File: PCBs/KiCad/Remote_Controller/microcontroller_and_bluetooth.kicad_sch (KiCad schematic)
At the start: 19 parts, among them J201 USB_C_Receptacle_USB2.0_16P, Q201 SS8050-G, Q202 SS8050-G, SW201 SW_Push, U201 USBLC6-2SC6, U202 ESP32-WROOM-32E, U203 CH340C

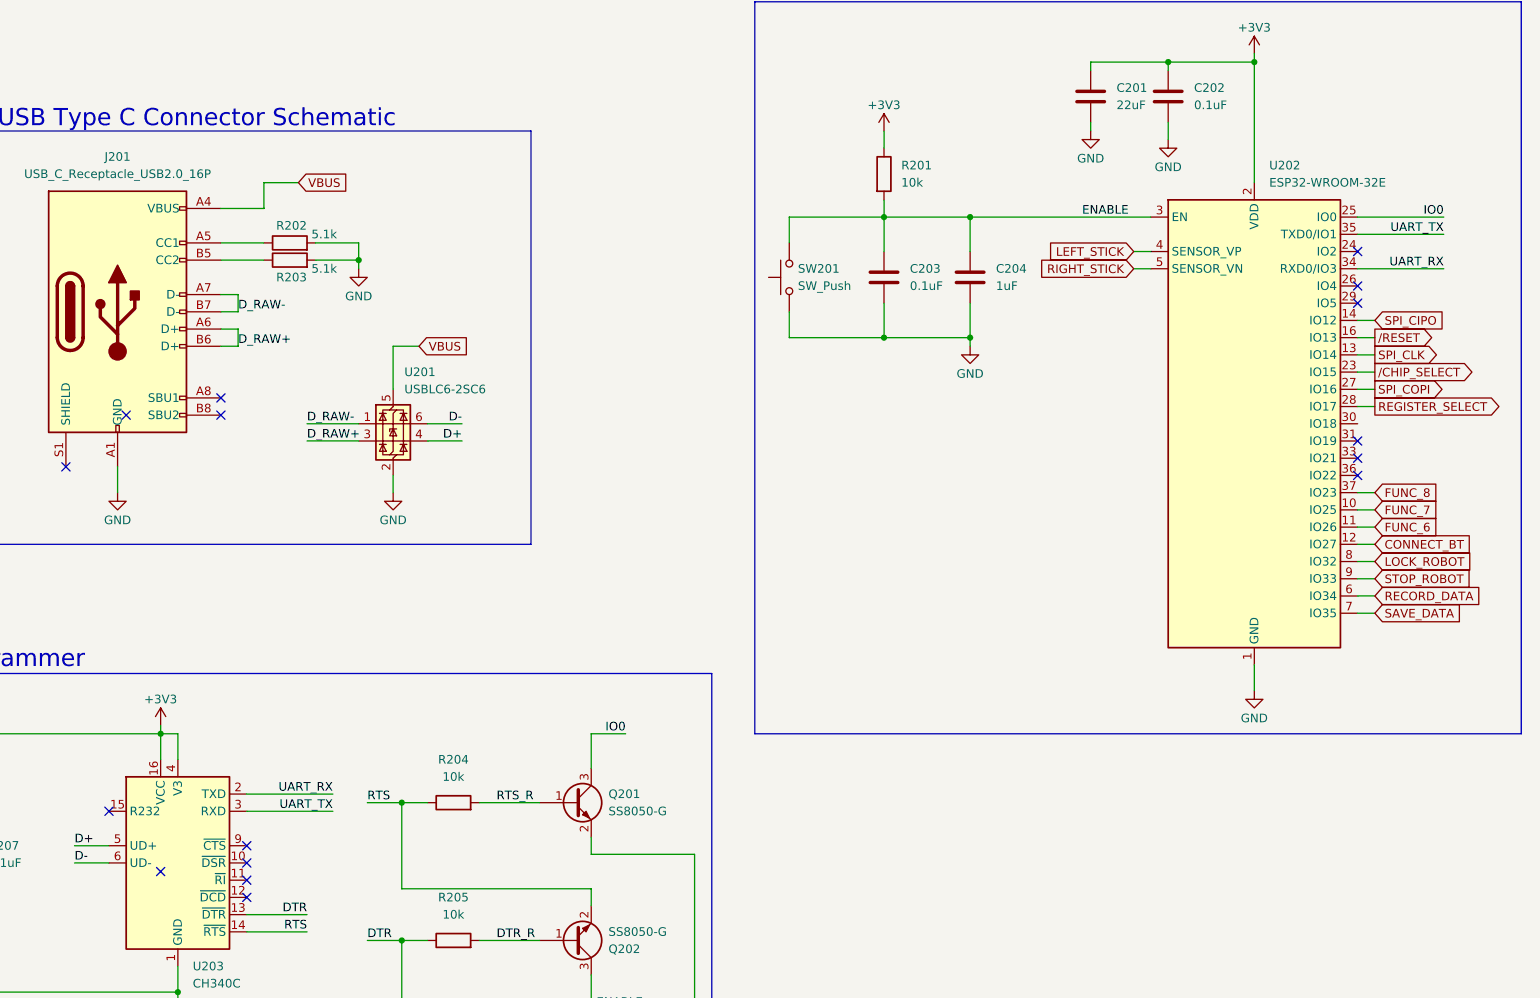
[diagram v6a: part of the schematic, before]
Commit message: Add Joystick footprint and passed ERC
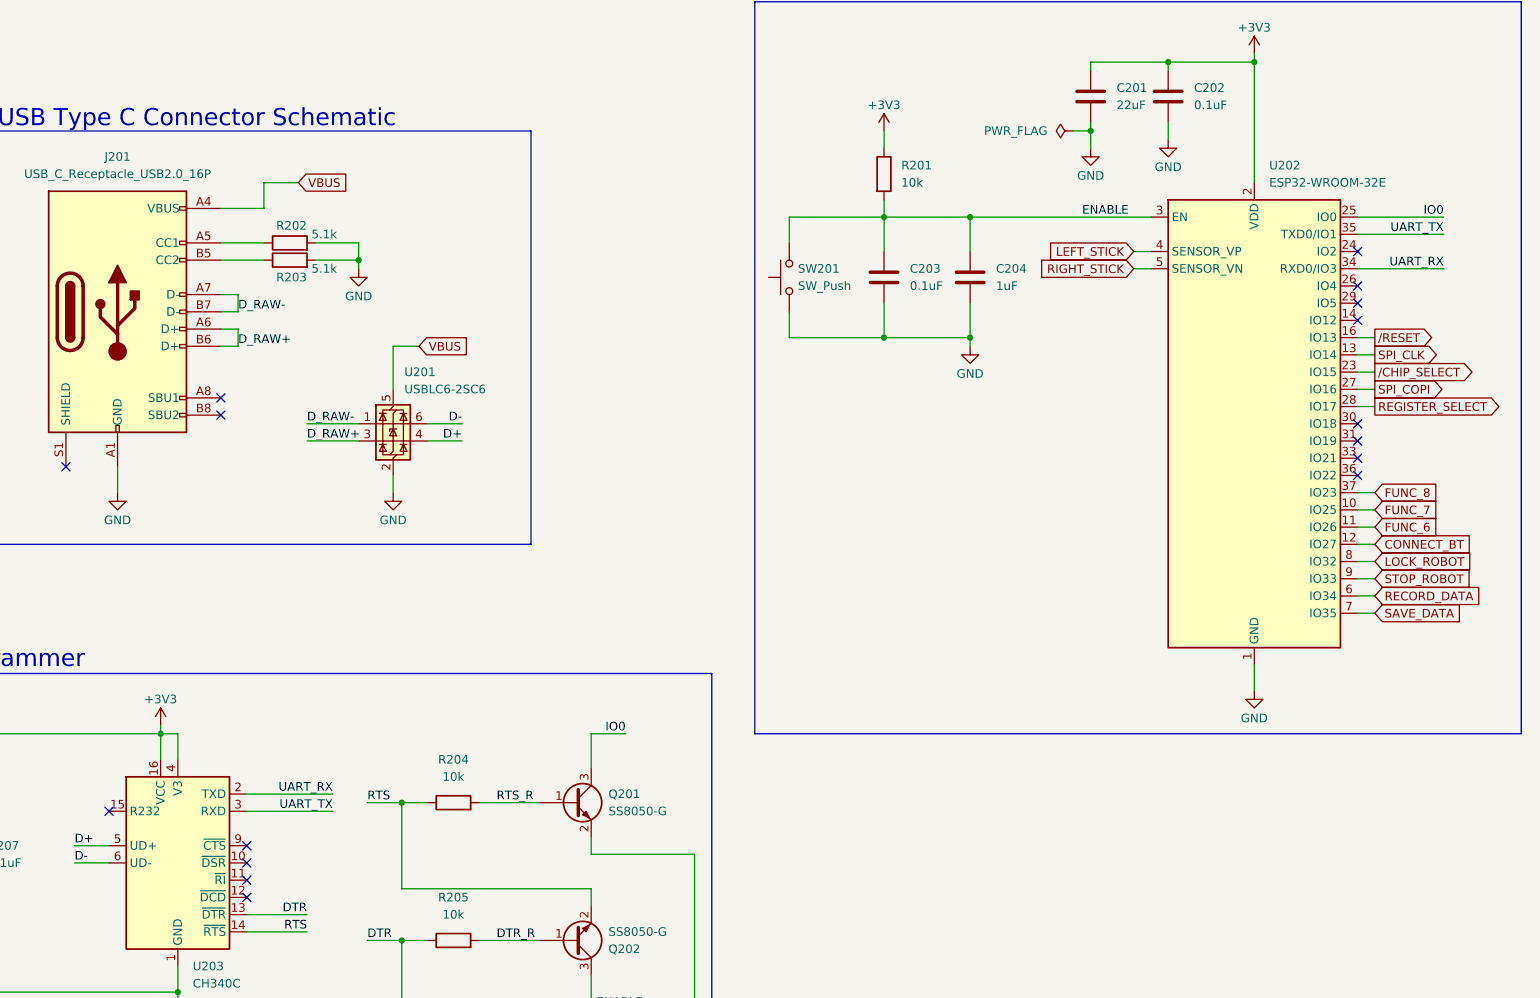
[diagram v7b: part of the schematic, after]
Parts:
- SW201: footprint (none) -> Button_Switch_SMD:SW_Tactile_SPST_NO_Straight_CK_PTS636Sx25SMTRLFS
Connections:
- net SPI_CIPO: no longer names the net of U202.14 (IO12)
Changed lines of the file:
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@@
 	(paper "A4")
+	(junction
+		(at 213.36 49.53)
+		(diameter 0)
+		(color 0 0 0 0)
+	)
 	(junction
 		(at 34.29 166.37)
@@
 	)
 	(no_connect
+		(at 252.73 77.47)
+	)
+	(no_connect
 		(at 88.9 157.48)
 	)
@@
 	)
 	(no_connect
-		(at 76.2 158.75)
+		(at 252.73 92.71)
 	)
 	(no_connect
@@
 	)
 	(no_connect
-		(at 71.12 91.44)
-	)
-	(no_connect
 		(at 88.9 162.56)
 	)
@@
 	(wire
 		(pts
+			(xy 213.36 49.53) (xy 213.36 52.07)
+		)
+		(stroke
+			(width 0)
+			(type default)
+		)
+	)
+	(wire
+		(pts
 			(xy 34.29 176.53) (xy 78.74 176.53)
 		)
@@
 	(wire
 		(pts
+			(xy 210.82 49.53) (xy 213.36 49.53)
+		)
+		(stroke
+			(width 0)
+			(type default)
+		)
+	)
+	(wire
+		(pts
 			(xy 34.29 160.02) (xy 34.29 166.37)
 		)
@@
 		(pts
 			(xy 213.36 40.64) (xy 213.36 39.37)
-		)
-		(stroke
-			(width 0)
-			(type default)
-		)
-	)
-	(wire
-		(pts
-			(xy 252.73 77.47) (xy 255.27 77.47)
 		)
 		(stroke
@@
 		(property "Intersheetrefs" "${INTERSHEET_REFS}"
 			(at 265.4519 105.41 0)
-			(effects
-				(font
-					(size 1.27 1.27)
-				)
-				(justify left)
-				(hide yes)
-			)
-		)
-	)
-	(global_label "SPI_CIPO"
-		(shape input)
-		(at 255.27 77.47 0)
-		(fields_autoplaced yes)
-		(effects
-			(font
-				(size 1.27 1.27)
-			)
-			(justify left)
-		)
-		(property "Intersheetrefs" "${INTERSHEET_REFS}"
-			(at 266.7824 77.47 0)
 			(effects
 				(font
@@
 	(symbol
 		(lib_id "power:GND")
-		(at 213.36 49.53 0)
+		(at 213.36 52.07 0)
 		(unit 1)
 		(exclude_from_sim no)
@@
 		(dnp no)
 		(property "Reference" "#PWR013"
-			(at 213.36 55.88 0)
+			(at 213.36 58.42 0)
 			(effects
 				(font
@@
 		)
 		(property "Value" "GND"
-			(at 213.36 53.594 0)
+			(at 213.36 56.134 0)
 			(effects
 				(font
@@
 		)
 		(property "Footprint" ""
-			(at 213.36 49.53 0)
+			(at 213.36 52.07 0)
 			(effects
 				(font
@@
 		)
 		(property "Datasheet" ""
-			(at 213.36 49.53 0)
+			(at 213.36 52.07 0)
 			(effects
 				(font
@@
 		)
 		(property "Description" "Power symbol creates a global label with name \"GND\" , ground"
-			(at 213.36 49.53 0)
+			(at 213.36 52.07 0)
 			(effects
 				(font
@@
 			)
 		)
-		(property "Footprint" ""
+		(property "Footprint" "Button_Switch_SMD:SW_Tactile_SPST_NO_Straight_CK_PTS636Sx25SMTRLFS"
 			(at 163.83 71.12 0)
 			(effects
@@
 					(unit 1)
 				)
+			)
+		)
+	)
+	(symbol
+		(lib_id "power:PWR_FLAG")
+		(at 210.82 49.53 90)
+		(unit 1)
+		(exclude_from_sim no)
+		(in_bom yes)
+		(on_board yes)
+		(dnp no)
+		(fields_autoplaced yes)
+		(property "Reference" "#FLG0105"
+			(at 208.915 49.53 0)
+			(effects
+				(font
+					(size 1.27 1.27)
+				)
+				(hide yes)
+			)
+		)
+		(property "Value" "PWR_FLAG"
+			(at 207.01 49.5299 90)
+			(effects
+				(font
+					(size 1.27 1.27)
+				)
+				(justify left)
+			)
+		)
+		(property "Footprint" ""
+			(at 210.82 49.53 0)
+			(effects
+				(font
+					(size 1.27 1.27)
+				)
+				(hide yes)
+			)
+		)
+		(property "Datasheet" "~"
+			(at 210.82 49.53 0)
+			(effects
+				(font
+					(size 1.27 1.27)
+				)
+				(hide yes)
+			)
+		)
+		(property "Description" "Special symbol for telling ERC where power comes from"
+			(at 210.82 49.53 0)
+			(effects
+				(font
+					(size 1.27 1.27)
+				)
+				(hide yes)
+			)
+		)
+		(pin "1"
+		)
+		(instances
+			(project "Remote_Controller"
+				(path "/7afb5074-6b77-4607-a5eb-938c2def45ba/79876373-4fa4-487a-ae74-dfa9ff220508"
+					(reference "#FLG0105")
+					(unit 1)
+				)

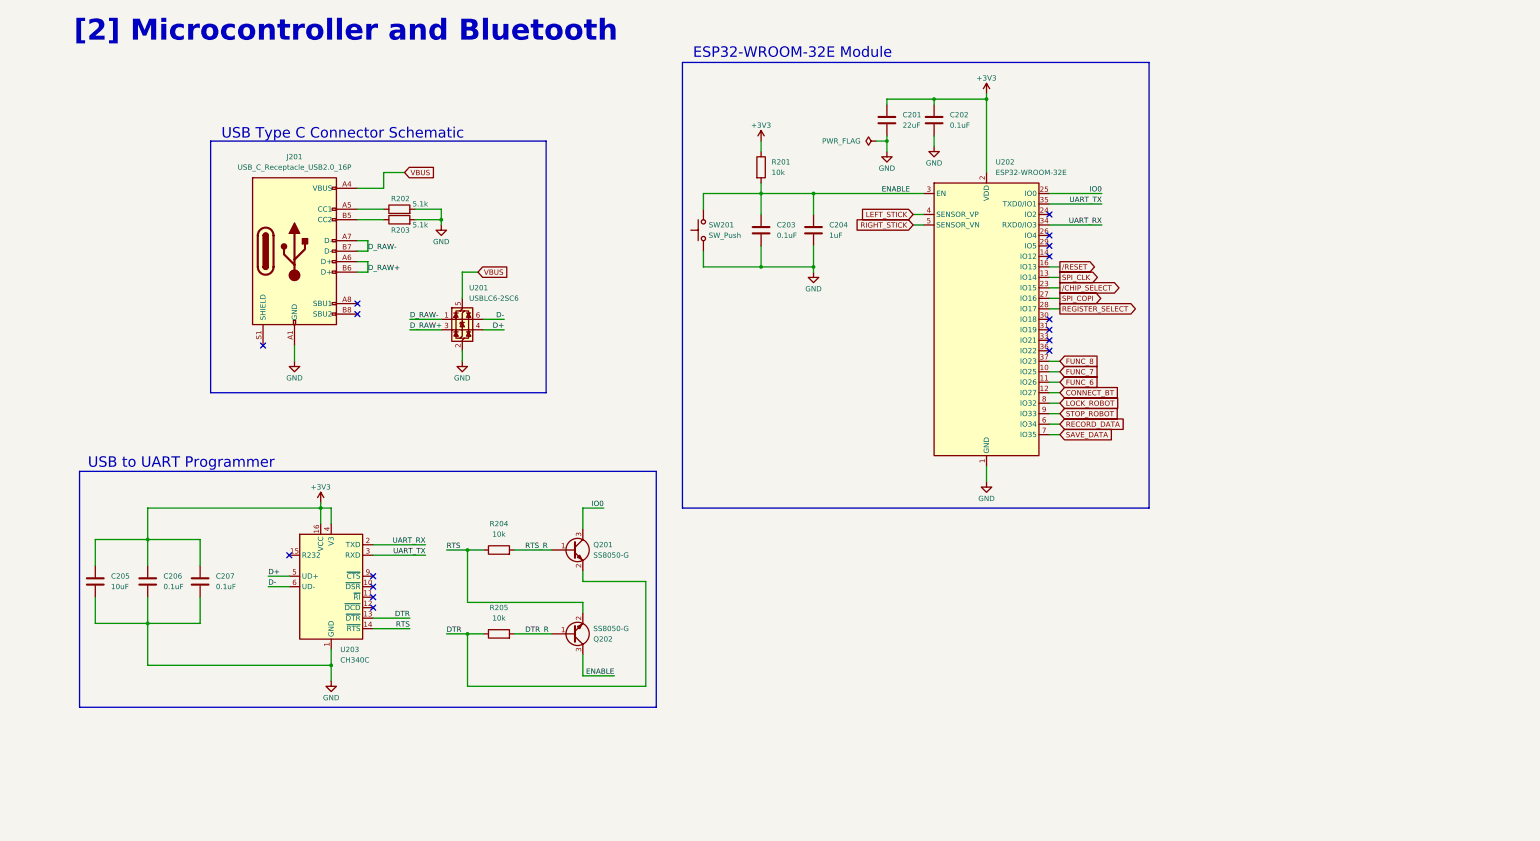
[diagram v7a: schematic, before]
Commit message: Reduced size of capacitor C201 to 0603 and corrected CH340 cap decoupler circuit, also improved PCB layout
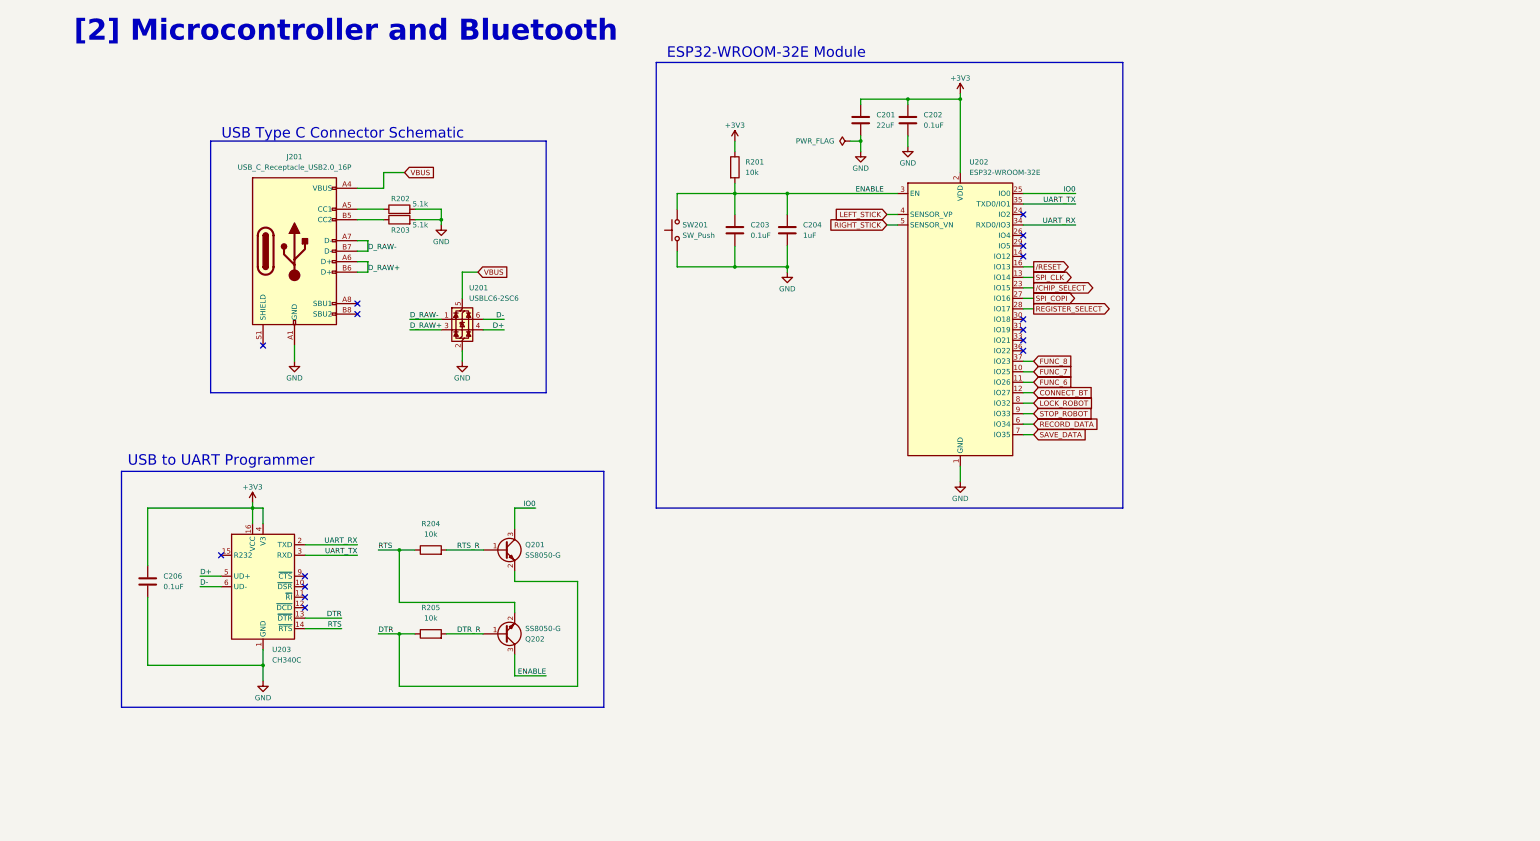
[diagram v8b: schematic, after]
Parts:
- removed C205: 10uF, Capacitor_SMD:C_0805_2012Metric, symbol Device:C
- removed C207: 0.1uF, Capacitor_SMD:C_0402_1005Metric, symbol Device:C
- C201: footprint Capacitor_SMD:C_1206_3216Metric -> Capacitor_SMD:C_0603_1608Metric
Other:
- moved on the sheet: C201, C202, C203, C204, Q201, Q202, R201, R204, R205, SW201, U202, U203
